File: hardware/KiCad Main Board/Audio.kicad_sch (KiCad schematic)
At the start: 35 parts, among them J6 SPK_CONN_INT, J7 SPK_2.5MM SJ1-2503A, J8 MIC_3.5MM PJ-307C, U12 TLV320AIC3100, U8 SPH0645LM4H

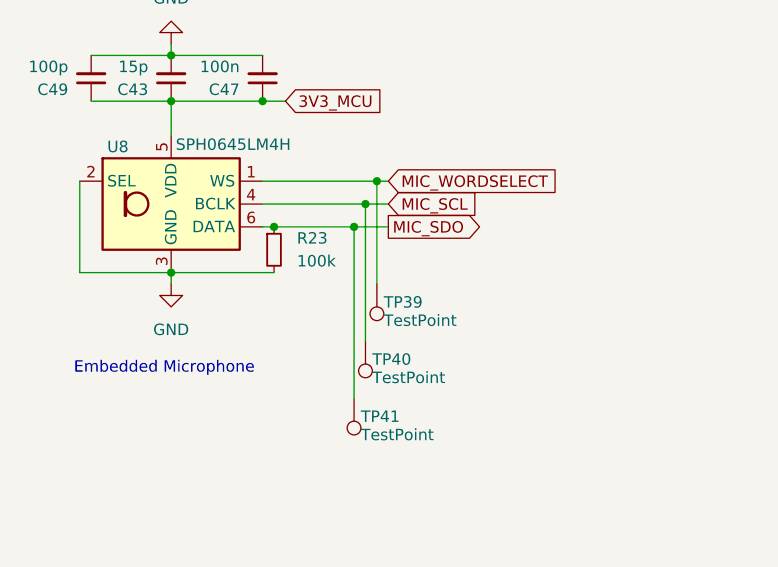
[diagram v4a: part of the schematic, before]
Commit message: finished routing, working on DRC
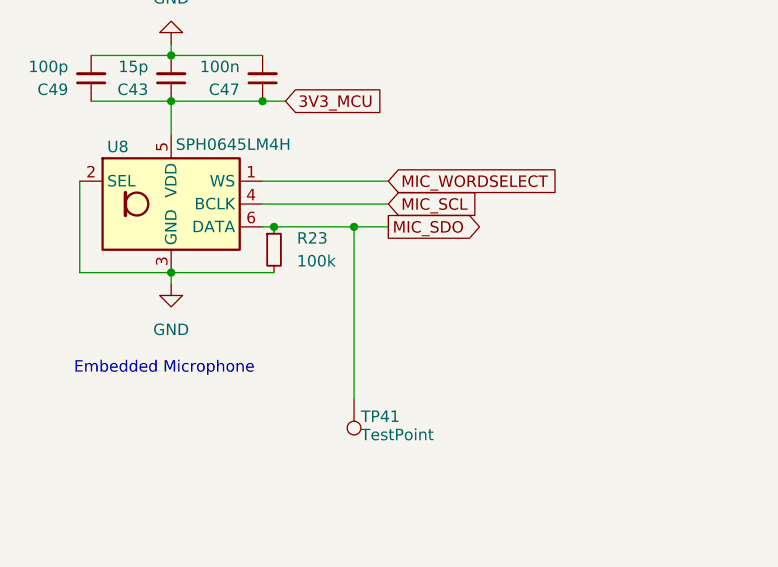
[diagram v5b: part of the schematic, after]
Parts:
- removed TP39, TP40: TestPoint, TestPoint:TestPoint_Pad_D1.0mm, symbol Connector:TestPoint
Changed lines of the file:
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@@
 	)
 	(junction
-		(at 73.66 54.61)
-		(diameter 0)
-		(color 0 0 0 0)
-	)
-	(junction
 		(at 198.12 90.17)
 		(diameter 0)
@@
 	)
 	(junction
-		(at 72.39 57.15)
-		(diameter 0)
-		(color 0 0 0 0)
-	)
-	(junction
 		(at 163.83 45.72)
 		(diameter 0)
@@
 	(wire
 		(pts
-			(xy 73.66 54.61) (xy 60.96 54.61)
+			(xy 60.96 54.61) (xy 74.93 54.61)
 		)
 		(stroke
@@
 	(wire
 		(pts
-			(xy 72.39 57.15) (xy 72.39 72.39)
-		)
-		(stroke
-			(width 0)
-			(type default)
-		)
-	)
-	(wire
-		(pts
 			(xy 218.44 77.47) (xy 232.41 77.47)
 		)
@@
 	(wire
 		(pts
-			(xy 73.66 54.61) (xy 73.66 66.04)
-		)
-		(stroke
-			(width 0)
-			(type default)
-		)
-	)
-	(wire
-		(pts
 			(xy 251.46 90.17) (xy 220.98 90.17)
 		)
@@
 	(wire
 		(pts
-			(xy 72.39 57.15) (xy 60.96 57.15)
+			(xy 60.96 57.15) (xy 74.93 57.15)
 		)
 		(stroke
@@
 	(wire
 		(pts
-			(xy 74.93 57.15) (xy 72.39 57.15)
-		)
-		(stroke
-			(width 0)
-			(type default)
-		)
-	)
-	(wire
-		(pts
 			(xy 62.23 59.69) (xy 60.96 59.69)
 		)
@@
 	(wire
 		(pts
-			(xy 74.93 54.61) (xy 73.66 54.61)
-		)
-		(stroke
-			(width 0)
-			(type default)
-		)
-	)
-	(wire
-		(pts
 			(xy 201.93 44.45) (xy 201.93 48.26)
 		)
@@
 	)
 	(symbol
-		(lib_id "Connector:TestPoint")
-		(at 72.39 72.39 180)
-		(unit 1)
-		(exclude_from_sim no)
-		(in_bom yes)
-		(on_board yes)
-		(dnp no)
-		(property "Reference" "TP40"
-			(at 73.152 74.422 0)
-			(effects
-				(font
-					(size 1.27 1.27)
-				)
-				(justify right)
-			)
-		)
-		(property "Value" "TestPoint"
-			(at 73.152 76.454 0)
-			(effects
-				(font
-					(size 1.27 1.27)
-				)
-				(justify right)
-			)
-		)
-		(property "Footprint" "TestPoint:TestPoint_Pad_D1.0mm"
-			(at 67.31 72.39 0)
-			(effects
-				(font
-					(size 1.27 1.27)
-				)
-				(hide yes)
-			)
-		)
-		(property "Datasheet" "~"
-			(at 67.31 72.39 0)
-			(effects
-				(font
-					(size 1.27 1.27)
-				)
-				(hide yes)
-			)
-		)
-		(property "Description" "test point"
-			(at 72.39 72.39 0)
-			(effects
-				(font
-					(size 1.27 1.27)
-				)
-				(hide yes)
-			)
-		)
-		(pin "1"
-		)
-		(instances
-			(project "OSS Radio Hardware Design"
-				(path "/fd5c68a7-f5d0-4135-a258-bde3ebf63307/1fea53e1-bad3-4fc0-9492-4b8e0f78b13e"
-					(reference "TP40")
-					(unit 1)
-				)
-			)
-		)
-	)
-	(symbol
 		(lib_id "Diode:ESD9B3.3ST5G")
 		(at 167.64 109.22 270)
@@
 					(unit 1)
 				)
-			)
-		)
-	)
-	(symbol
-		(lib_id "Connector:TestPoint")
-		(at 73.66 66.04 180)
-		(unit 1)
-		(exclude_from_sim no)
-		(in_bom yes)
-		(on_board yes)
-		(dnp no)
-		(property "Reference" "TP39"
-			(at 74.422 68.072 0)
-			(effects
-				(font
-					(size 1.27 1.27)
-				)
-				(justify right)
-			)
-		)
-		(property "Value" "TestPoint"
-			(at 74.422 70.104 0)
-			(effects
-				(font
-					(size 1.27 1.27)
-				)
-				(justify right)
-			)
-		)
-		(property "Footprint" "TestPoint:TestPoint_Pad_D1.0mm"
-			(at 68.58 66.04 0)
-			(effects
-				(font
-					(size 1.27 1.27)
-				)
-				(hide yes)
-			)
-		)
-		(property "Datasheet" "~"
-			(at 68.58 66.04 0)
-			(effects
-				(font
-					(size 1.27 1.27)
-				)
-				(hide yes)
-			)
-		)
-		(property "Description" "test point"
-			(at 73.66 66.04 0)
-			(effects
-				(font
-					(size 1.27 1.27)
-				)
-				(hide yes)
-			)
-		)
-		(pin "1"
-		)
-		(instances
-			(project "OSS Radio Hardware Design"
-				(path "/fd5c68a7-f5d0-4135-a258-bde3ebf63307/1fea53e1-bad3-4fc0-9492-4b8e0f78b13e"
-					(reference "TP39")
-					(unit 1)
-				)

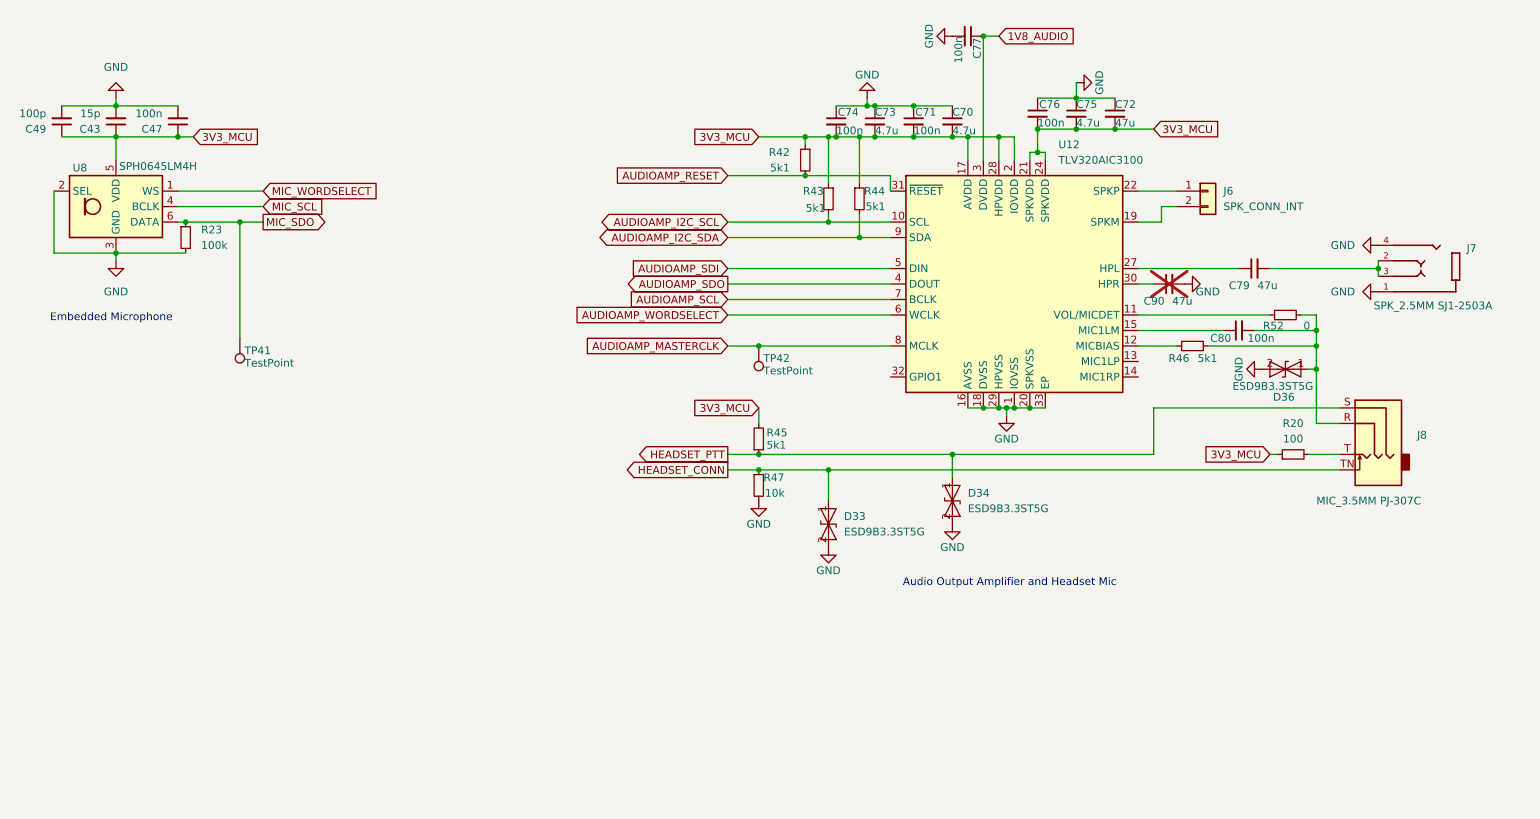
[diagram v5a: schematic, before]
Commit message: made audio amp power swichable
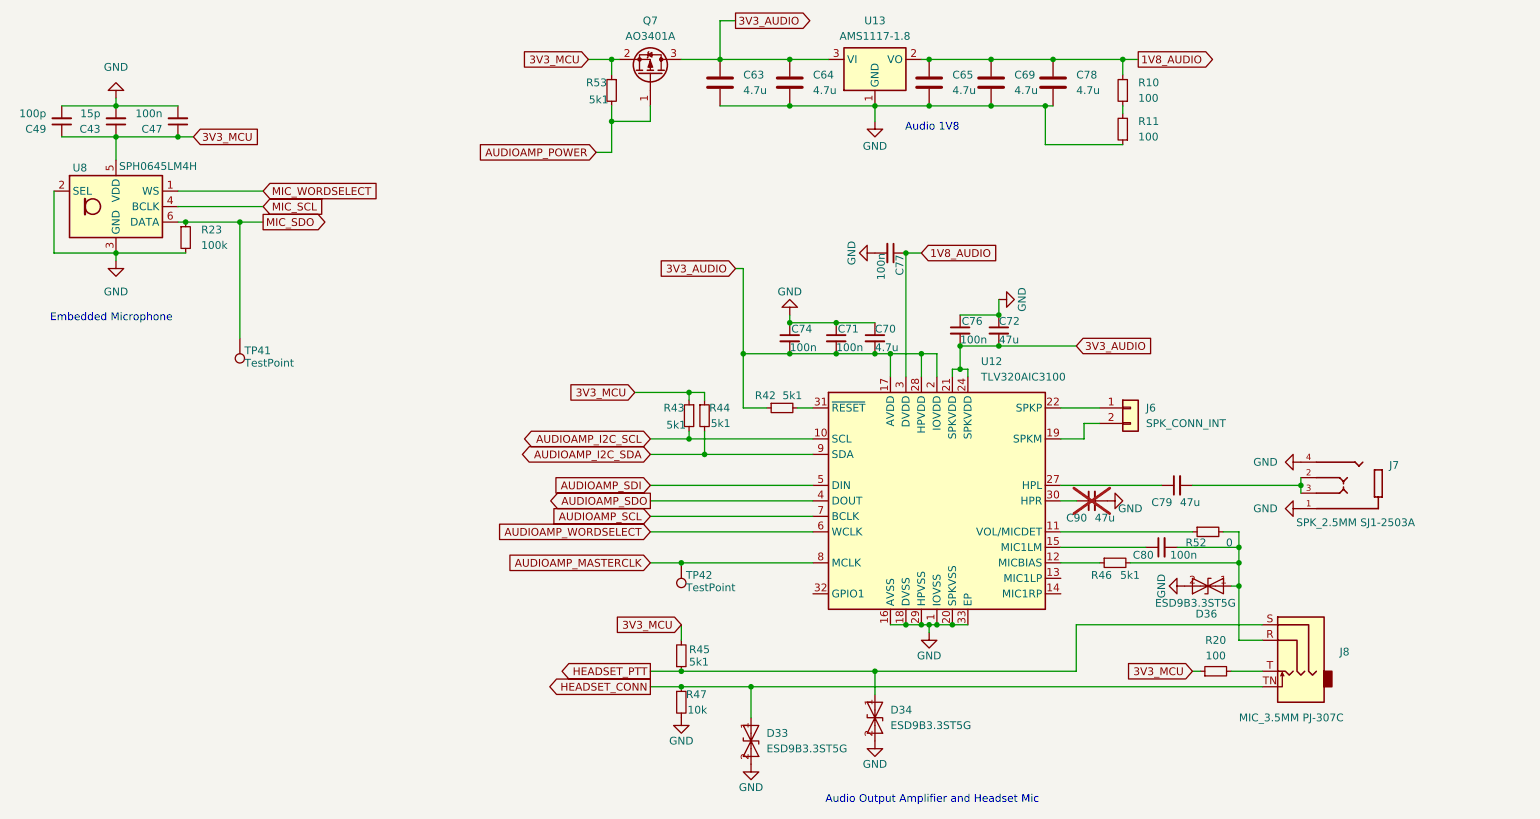
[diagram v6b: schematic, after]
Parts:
- removed C73, C75: 4.7u, Capacitor_SMD:C_0603_1608Metric_Pad1.08x0.95mm_HandSolder, symbol Device:C_Small
- added C63, C64, C65, C69, C78: 4.7u, Capacitor_SMD:C_0603_1608Metric_Pad1.08x0.95mm_HandSolder, symbol Device:C
- added Q7: AO3401A, Package_TO_SOT_SMD:SOT-23, symbol Transistor_FET:AO3401A
- added R10, R11: 100, Resistor_SMD:R_0603_1608Metric_Pad0.98x0.95mm_HandSolder, symbol Device:R_Small
- added R53: 5k1, Resistor_SMD:R_0603_1608Metric_Pad0.98x0.95mm_HandSolder, symbol Device:R_Small
- added U13: AMS1117-1.8, Package_TO_SOT_SMD:SOT-223-3_TabPin2, symbol Regulator_Linear:NCP1117-1.8_SOT223
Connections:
- net 1V8_AUDIO: now also C65.2, C69.2, C78.2, R10.2, U13.2 (VO)
- net 3V3_MCU: now also Q7.2 (S), R53.1; no longer C70.2, C71.2, C72.2, C74.2, C76.2, R42.1, U12.17 (AVDD), U12.2 (IOVDD), U12.21 (SPKVDD), U12.24 (SPKVDD), U12.28 (HPVDD)
- net GND: now also C63.1, C64.1, C65.1, C69.1, C78.1, R11.1, U13.1 (GND)
- net AUDIOAMP_RESET: no longer names the net of R42.2, U12.31 (~{RESET})
- new net: R10.1, R11.2
- new net 3V3_AUDIO: C63.2, C64.2, C70.2, C71.2, C72.2, C74.2, C76.2, Q7.3 (D), R42.1, U12.17 (AVDD), U12.2 (IOVDD), U12.21 (SPKVDD), U12.24 (SPKVDD), U12.28 (HPVDD), U13.3 (VI)
- new net AUDIOAMP_POWER: Q7.1 (G), R53.2
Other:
- note added: "Audio 1V8"
- moved on the sheet: C70, C71, C72, C74, C76, C77, C79, C80, C90, D33, D34, D36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

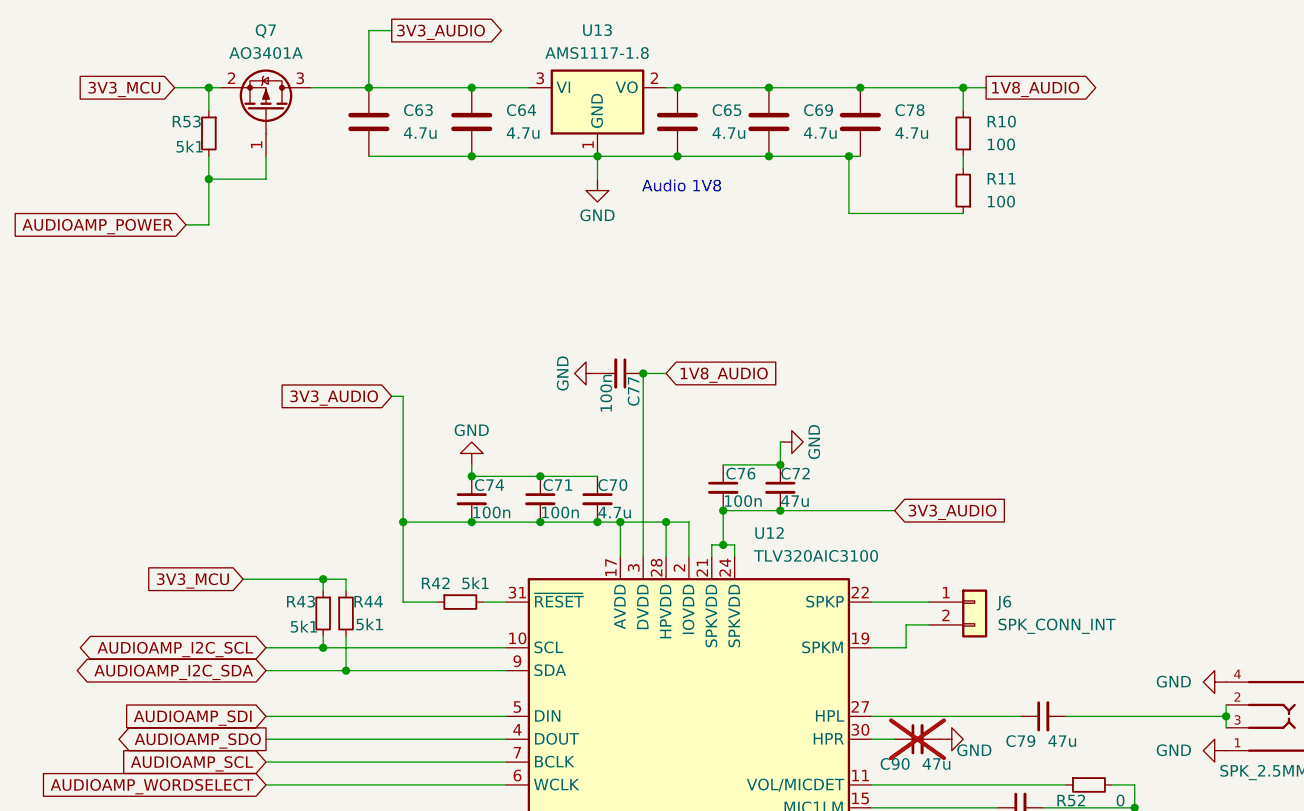
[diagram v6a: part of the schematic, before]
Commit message: finished routing changes for switching audio power
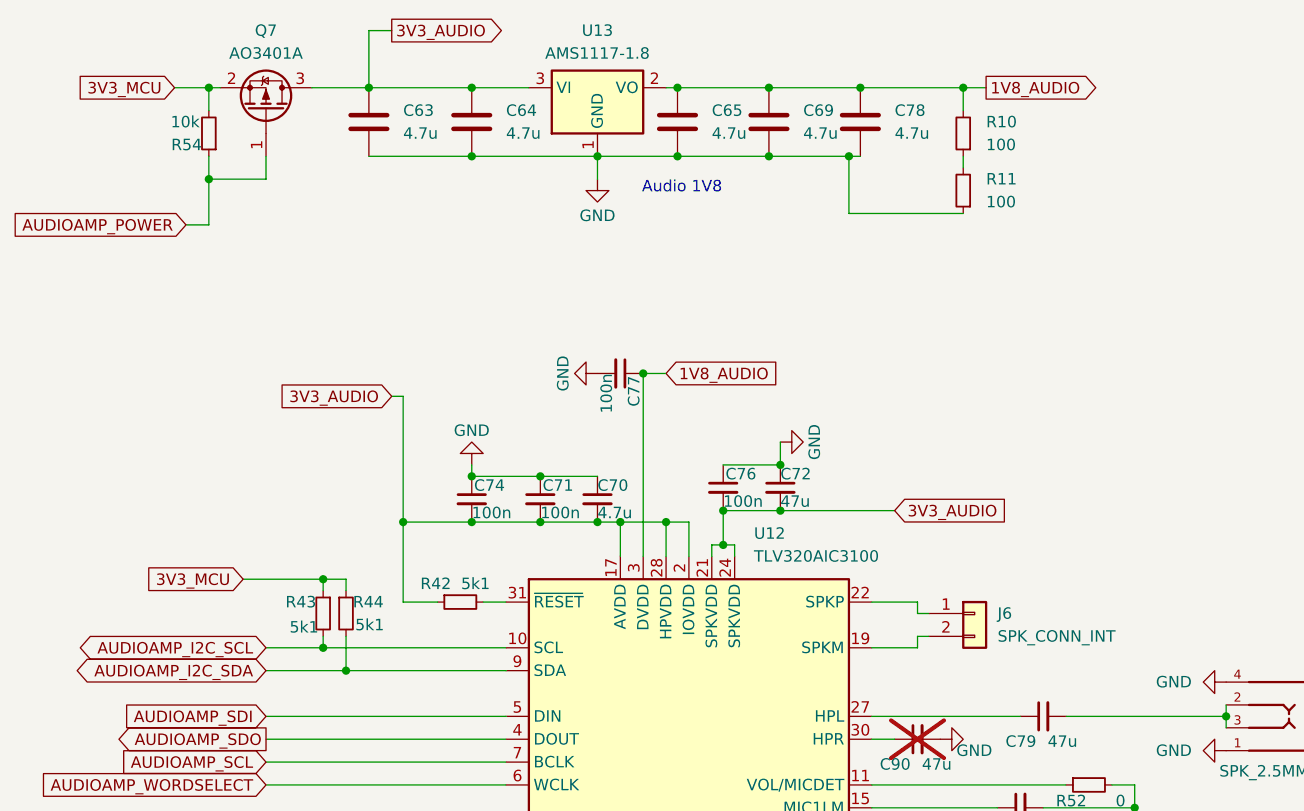
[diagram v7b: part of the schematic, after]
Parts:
- removed R53: 5k1, Resistor_SMD:R_0603_1608Metric_Pad0.98x0.95mm_HandSolder, symbol Device:R_Small
- added R54: 10k, Resistor_SMD:R_0603_1608Metric_Pad0.98x0.95mm_HandSolder, symbol Device:R_Small
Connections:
- net 3V3_MCU: now also R54.2
- net AUDIOAMP_POWER: now also R54.1
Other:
- moved on the sheet: J6
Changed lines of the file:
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@@
 	(wire
 		(pts
-			(xy 209.55 92.71) (xy 209.55 95.25)
+			(xy 210.82 93.98) (xy 210.82 95.25)
 		)
 		(stroke
@@
 	(wire
 		(pts
+			(xy 210.82 90.17) (xy 205.74 90.17)
+		)
+		(stroke
+			(width 0)
+			(type default)
+		)
+	)
+	(wire
+		(pts
+			(xy 210.82 91.44) (xy 210.82 90.17)
+		)
+		(stroke
+			(width 0)
+			(type default)
+		)
+	)
+	(wire
+		(pts
 			(xy 205.74 113.03) (xy 219.71 113.03)
 		)
@@
 	(wire
 		(pts
-			(xy 205.74 90.17) (xy 212.09 90.17)
+			(xy 210.82 91.44) (xy 212.09 91.44)
 		)
 		(stroke
@@
 	(wire
 		(pts
-			(xy 205.74 95.25) (xy 209.55 95.25)
+			(xy 205.74 95.25) (xy 210.82 95.25)
 		)
 		(stroke
@@
 	(wire
 		(pts
-			(xy 209.55 92.71) (xy 212.09 92.71)
+			(xy 210.82 93.98) (xy 212.09 93.98)
 		)
 		(stroke
@@
 	(symbol
 		(lib_id "Device:R_Small")
+		(at 132.08 38.1 180)
+		(unit 1)
+		(exclude_from_sim no)
+		(in_bom yes)
+		(on_board yes)
+		(dnp no)
+		(property "Reference" "R54"
+			(at 131.318 39.37 0)
+			(effects
+				(font
+					(size 1.27 1.27)
+				)
+				(justify left)
+			)
+		)
+		(property "Value" "10k"
+			(at 131.064 36.83 0)
+			(effects
+				(font
+					(size 1.27 1.27)
+				)
+				(justify left)
+			)
+		)
+		(property "Footprint" "Resistor_SMD:R_0603_1608Metric_Pad0.98x0.95mm_HandSolder"
+			(at 132.08 38.1 0)
+			(effects
+				(font
+					(size 1.27 1.27)
+				)
+				(hide yes)
+			)
+		)
+		(property "Datasheet" "~"
+			(at 132.08 38.1 0)
+			(effects
+				(font
+					(size 1.27 1.27)
+				)
+				(hide yes)
+			)
+		)
+		(property "Description" "Resistor, small symbol"
+			(at 132.08 38.1 0)
+			(effects
+				(font
+					(size 1.27 1.27)
+				)
+				(hide yes)
+			)
+		)
+		(pin "2"
+		)
+		(pin "1"
+		)
+		(instances
+			(project "OSS Radio Hardware Design"
+				(path "/fd5c68a7-f5d0-4135-a258-bde3ebf63307/1fea53e1-bad3-4fc0-9492-4b8e0f78b13e"
+					(reference "R54")
+					(unit 1)
+				)
+			)
+		)
+	)
+	(symbol
+		(lib_id "Device:R_Small")
 		(at 215.9 44.45 180)
 		(unit 1)
@@
 	)
 	(symbol
-		(lib_id "Device:R_Small")
-		(at 132.08 38.1 0)
-		(mirror y)
-		(unit 1)
-		(exclude_from_sim no)
-		(in_bom yes)
-		(on_board yes)
-		(dnp no)
-		(property "Reference" "R53"
-			(at 131.318 36.83 0)
-			(effects
-				(font
-					(size 1.27 1.27)
-				)
-				(justify left)
-			)
-		)
-		(property "Value" "5k1"
-			(at 131.572 39.624 0)
-			(effects
-				(font
-					(size 1.27 1.27)
-				)
-				(justify left)
-			)
-		)
-		(property "Footprint" "Resistor_SMD:R_0603_1608Metric_Pad0.98x0.95mm_HandSolder"
-			(at 132.08 38.1 0)
-			(effects
-				(font
-					(size 1.27 1.27)
-				)
-				(hide yes)
-			)
-		)
-		(property "Datasheet" "~"
-			(at 132.08 38.1 0)
-			(effects
-				(font
-					(size 1.27 1.27)
-				)
-				(hide yes)
-			)
-		)
-		(property "Description" "Resistor, small symbol"
-			(at 132.08 38.1 0)
-			(effects
-				(font
-					(size 1.27 1.27)
-				)
-				(hide yes)
-			)
-		)
-		(pin "2"
-		)
-		(pin "1"
-		)
-		(instances
-			(project "OSS Radio Hardware Design"
-				(path "/fd5c68a7-f5d0-4135-a258-bde3ebf63307/1fea53e1-bad3-4fc0-9492-4b8e0f78b13e"
-					(reference "R53")
-					(unit 1)
-				)
-			)
-		)
-	)
-	(symbol
 		(lib_id "Connector:TestPoint")
 		(at 71.12 78.74 180)
@@
 	(symbol
 		(lib_id "Connector_Generic:Conn_01x02")
-		(at 217.17 90.17 0)
+		(at 217.17 91.44 0)
 		(unit 1)
 		(exclude_from_sim no)
@@
 		(fields_autoplaced yes)
 		(property "Reference" "J6"
-			(at 219.71 90.1699 0)
+			(at 219.71 91.4399 0)
 			(effects
 				(font
@@
 		)
 		(property "Value" "SPK_CONN_INT"
-			(at 219.71 92.7099 0)
+			(at 219.71 93.9799 0)
 			(effects
 				(font
@@
 		)
 		(property "Footprint" "Connector_JST:JST_PH_S2B-PH-K_1x02_P2.00mm_Horizontal"
-			(at 217.17 90.17 0)
+			(at 217.17 91.44 0)
 			(effects
 				(font
@@
 		)
 		(property "Datasheet" "~"
-			(at 217.17 90.17 0)
+			(at 217.17 91.44 0)
 			(effects
 				(font
@@
 		)
 		(property "Description" "Generic connector, single row, 01x02, script generated (kicad-library-utils/schlib/autogen/connector/)"
-			(at 217.17 90.17 0)
+			(at 217.17 91.44 0)
 			(effects
 				(font
